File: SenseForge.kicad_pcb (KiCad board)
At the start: 2 copper layers, 11 parts, among them J1 SHTC3, J2 PIR, J3 BH1750, J4 I2C, SW1 custom_button

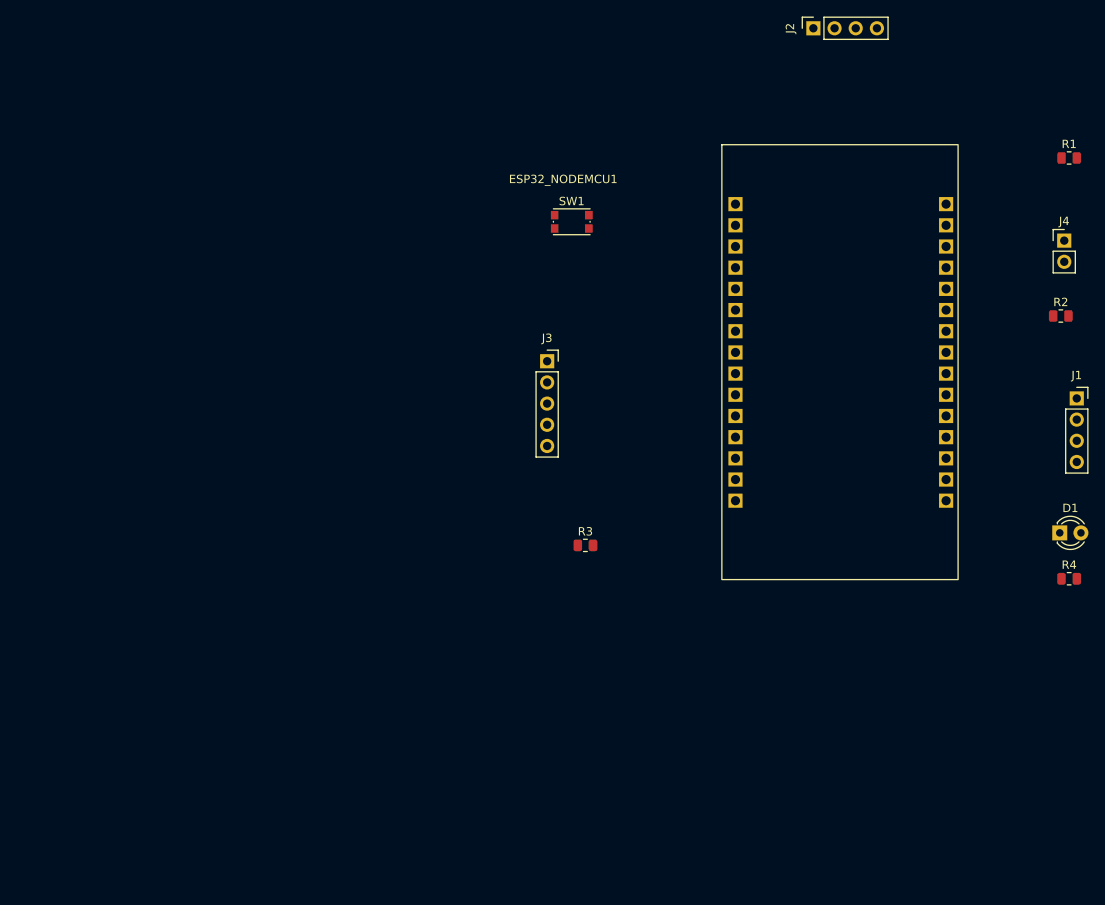
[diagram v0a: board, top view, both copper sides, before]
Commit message: update: latest SenseForge PCB and schematic changes
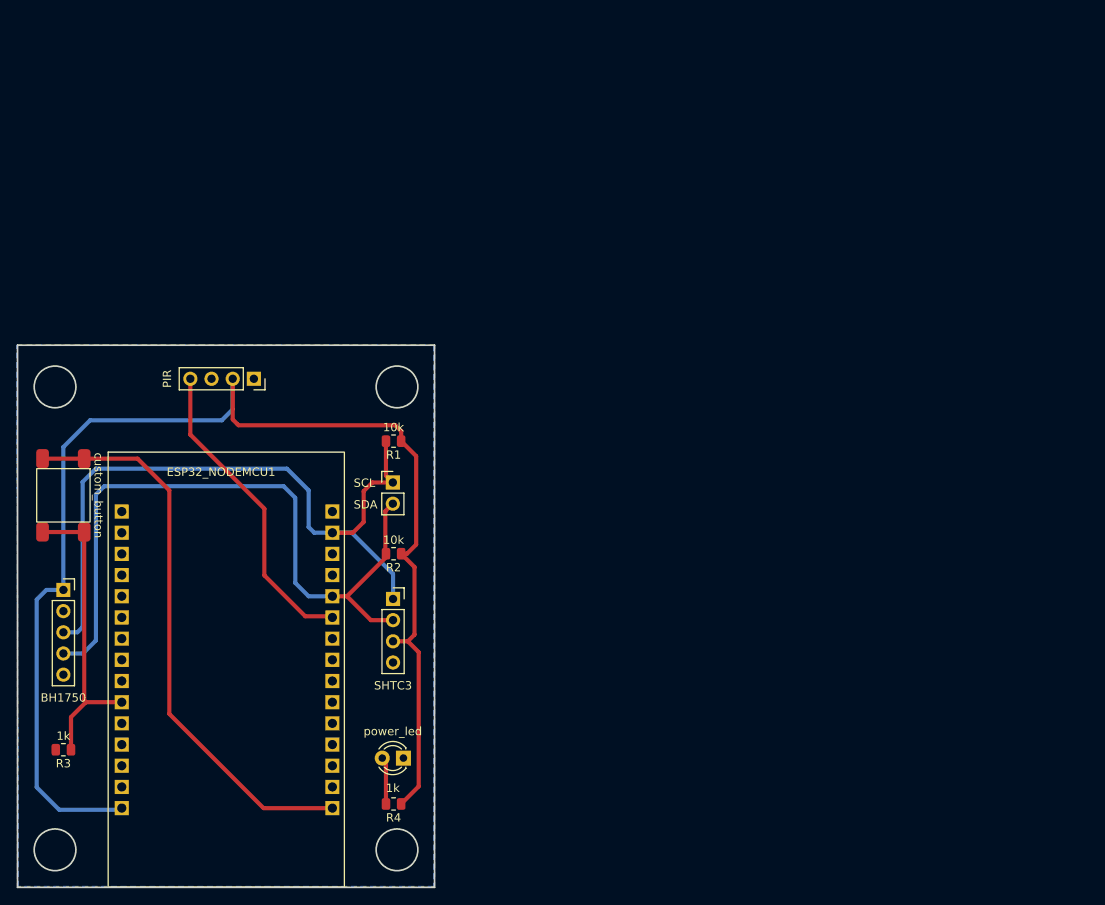
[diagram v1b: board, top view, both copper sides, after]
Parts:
- SW1: footprint Button_Switch_SMD:SW_Push_1P1T_NO_CK_KMR2 -> _myLibrary:button_push_sms
- moved R1 87.8 mm to (90.1, 96.5), turned to 180 degrees
- moved J4 85.6 mm to (90.0, 101.5)
- moved J1 85.4 mm to (90.0, 115.4)
- moved R4 85.4 mm to (90.1, 140.0), turned to 180 degrees
- moved R2 84.9 mm to (90.1, 110.0), turned to 180 degrees
- moved D1 83.2 mm to (91.3, 134.5), turned to 180 degrees
- moved ESP32_NODEMCU1 82.3 mm to (55.8, 98.0)
- moved J2 79.2 mm to (73.3, 89.0), turned to -90 degrees
- moved SW1 69.2 mm to (50.5, 103.0), turned to -90 degrees
- moved R3 67.2 mm to (50.5, 133.5), turned to 180 degrees
- moved J3 64.2 mm to (50.5, 114.3)
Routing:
- net 5V: track 0.00 -> 157.0 mm
- net SCL: track 0.00 -> 85.9 mm
- net SDA: track 0.00 -> 84.2 mm
- net 3V3: track 0.00 -> 67.8 mm
- net SIG_PIR: track 0.00 -> 37.5 mm
- net Net-(ESP32_NODEMCU1-D27): track 0.00 -> 36.2 mm
- net Net-(D1-A): track 0.00 -> 5.68 mm
- added copper zone on B.Cu, net GND
- added copper zone on F.Cu, net GND
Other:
- board outline added: 50 x 65 mm
- board text added: "SCL"
- board text added: "SDA"
